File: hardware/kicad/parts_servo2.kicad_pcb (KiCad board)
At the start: 2 copper layers, 37.3 x 17.5 mm, 50 parts, among them Q110 NFET-DUAL, Q120 NFET-DUAL, U1 MCP1703-3302, U100 RT9625A, U200 AS5050, U50 NRF51822, X60 16MHz

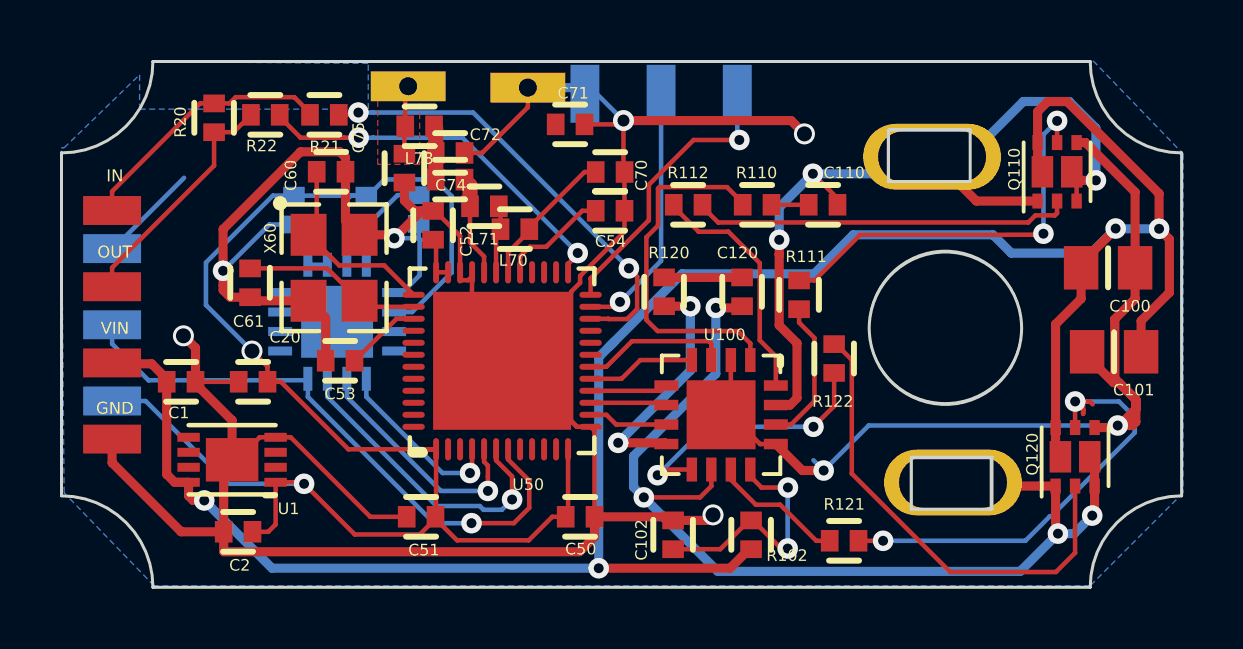
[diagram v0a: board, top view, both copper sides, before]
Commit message: Add pi filter to matching network.  Clean up routing and create parts_servo2.kicad_pcb with latest changes
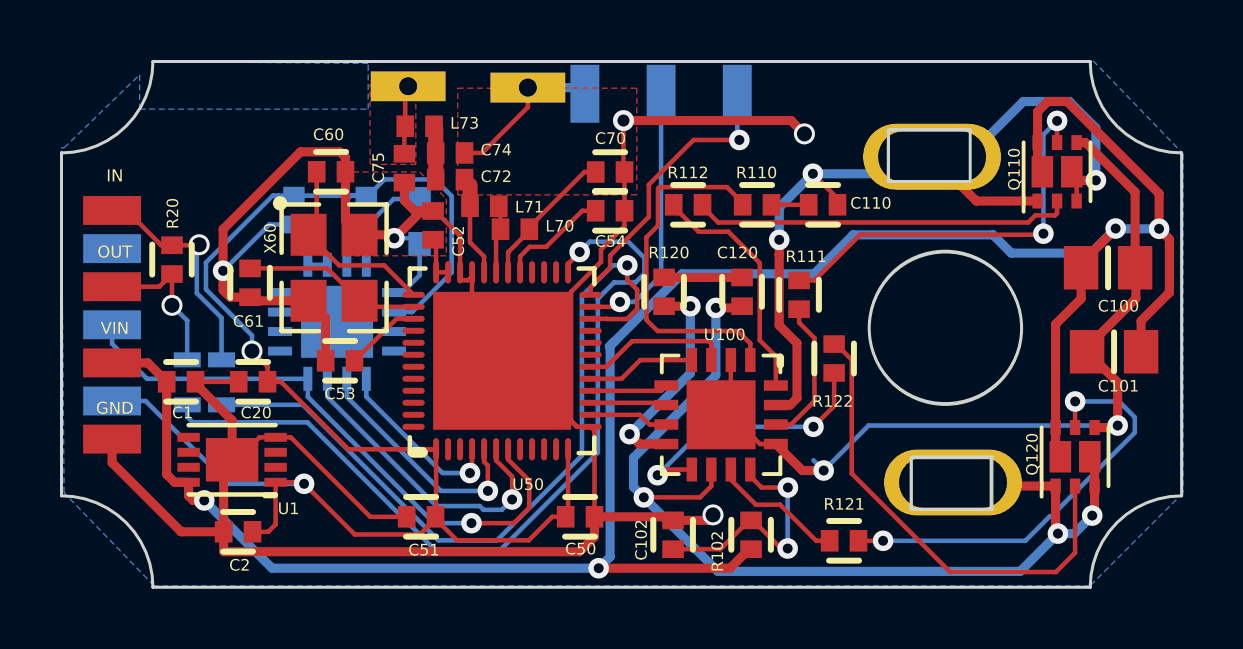
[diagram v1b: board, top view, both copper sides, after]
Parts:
- removed C71: np, parts_servo:0402-B
- C204: footprint parts_servo:0402-B -> Capacitors_SMD:C_0603
- R21, R22: footprint parts_servo:0402-B -> Resistors_SMD:R_0603; moved to B.Cu
- moved R21 9.55 mm to (135.1, 107.0), turned to 270 degrees
- moved R22 9.29 mm to (134.0, 107.0), turned to 270 degrees
- moved R20 4.93 mm to (133.5, 102.9)
- moved C204 0.40 mm to (141.7, 101.6)
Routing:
- net GND: track 152.4 -> 134.8 mm, vias 8 -> 7
- net /UNIPOLAR_OUTPUT: track 12.8 -> 28.5 mm, vias 2 -> 1
- net /UNIPOLAR_INPUT: track 15.0 -> 25.6 mm, vias 2 -> 1
- net Net-(JP2-Pad3): track 8.03 -> 5.44 mm, vias 0 -> 1
- net Net-(Q120-Pad5): track 16.4 -> 14.3 mm
- net Net-(JP2-Pad4): track 8.88 -> 7.60 mm, vias 0 -> 1
- net Net-(R120-Pad1): track 8.05 -> 7.34 mm
- added copper zone on F.Cu, net GND
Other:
- rule trace_min: 0.1524 -> 0.127
